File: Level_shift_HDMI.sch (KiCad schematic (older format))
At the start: 11 parts, among them U5 TXB0104RUT

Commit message: removed finished remarks
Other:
- note removed: "REMARK:Please unify convention of naming power supply labels.\nWe often use global labels. Always check that the name is exactly the same."
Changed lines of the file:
@@
 Wire Wire Line
 	7050 2150 7300 2150
-Text Notes 3650 975  0    50   ~ 0
-REMARK:Please unify convention of naming power supply labels.\nWe often use global labels. Always check that the name is exactly the same.
 $Comp
 L antmicroLogicTranslatorsLevelShifters:TXS0102YZPR U?

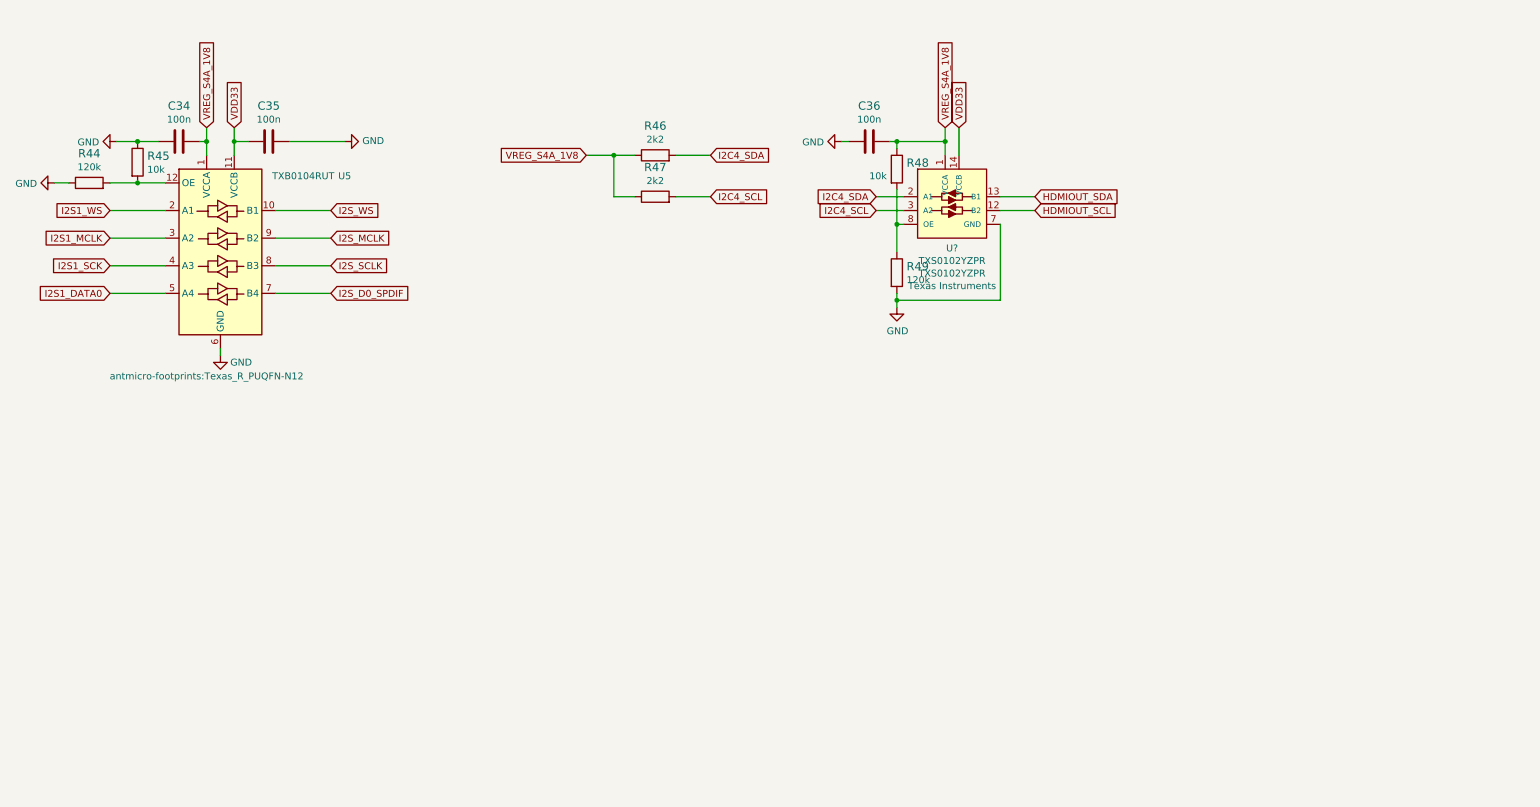
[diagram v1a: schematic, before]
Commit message: finished level shifting circuits for HDMI
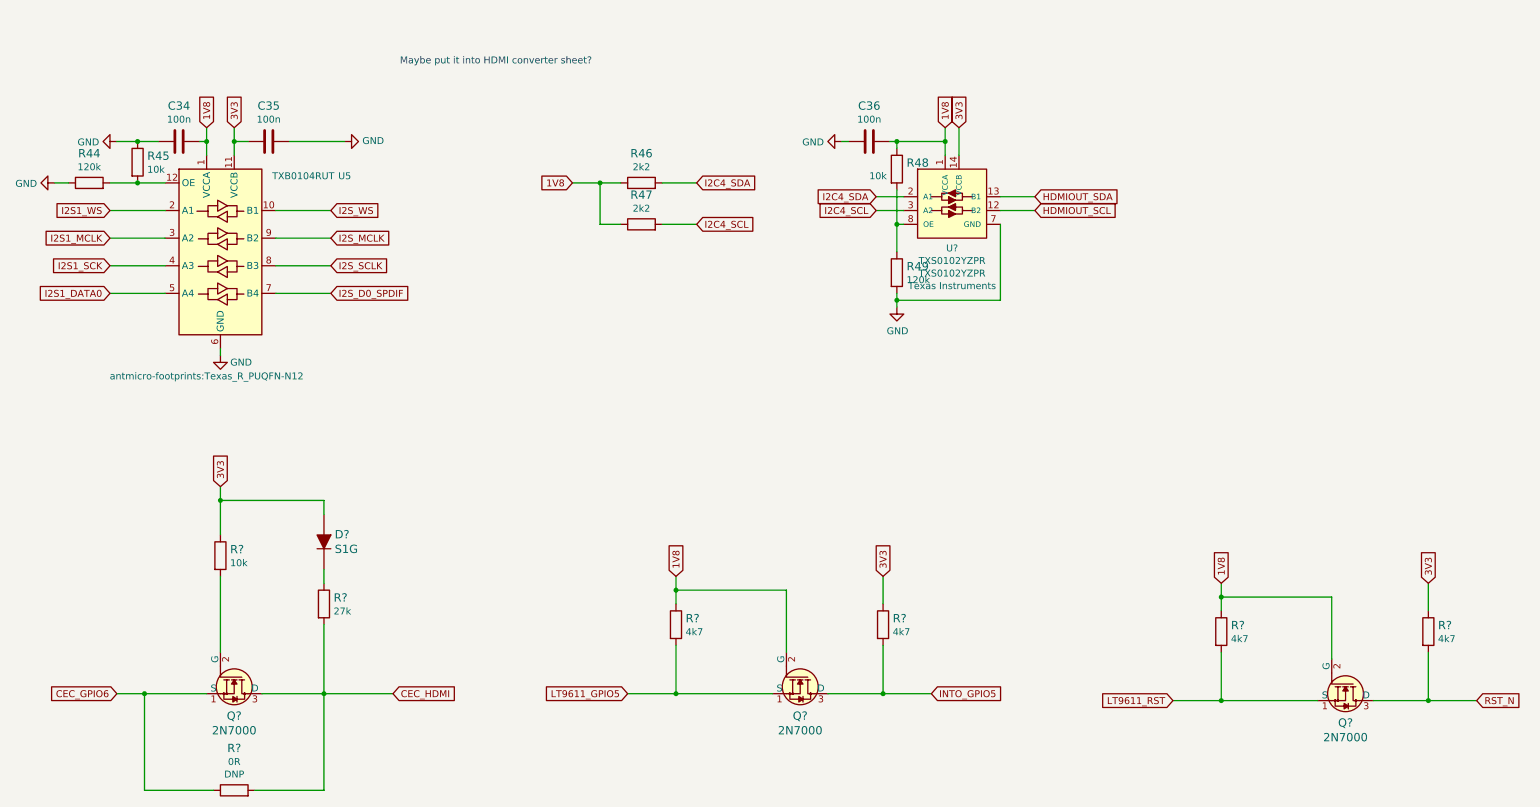
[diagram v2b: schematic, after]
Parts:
- added D?: S1G, antmicro-footprints:DO-214AC, symbol antmicroDiodesRectifiersSingle:S1G
- added Q? (x3): 2N7000, antmicro-footprints:TO-92-3, symbol antmicroTransistorsFETsMOSFETsSingle:2N7000
- added R? (x4): R_4k7_0402, antmicro-footprints:0402-res, symbol antmicroResistors0402:R_4k7_0402
- added R?: R_10k_0402, antmicro-footprints:0402-res, symbol antmicroResistors0402:R_10k_0402
- added R?: R_27k_0402, antmicro-footprints:0402-res, symbol antmicroResistors0402:R_27k_0402
- added R?: R_0R_0402, antmicro-footprints:0402-res, symbol antmicroResistors0402:R_0R_0402
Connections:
- net VDD33 renamed 3V3
- net 3V3: now also D?.A, R?.1, R?.1, R?.1
- net VREG_S4A_1V8 renamed 1V8
- net 1V8: now also Q?.2 (G), Q?.2 (G), R?.1, R?.1
- new net: Q?.2 (G), R?.2
- new net: D?.K, R?.1
- new net CEC_GPIO6: Q?.1 (S), R?.1
- new net CEC_HDMI: Q?.3 (D), R?.2, R?.2
- new net INTO_GPIO5: Q?.3 (D), R?.2
- new net LT9611_GPIO5: Q?.1 (S), R?.2
- new net LT9611_RST: Q?.1 (S), R?.2
- new net RST_N: Q?.3 (D), R?.2
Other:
- note added: "Maybe put it into HDMI converter sheet?\n"
- moved on the sheet: R46, R47

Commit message: Add local libs to fix CI
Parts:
- C34, C35, C36: footprint antmicro-footprints:0402-cap -> sa800u-baseboard-hw-footprints:0402-cap; symbol antmicroCapacitors0402:C_100n_0402 -> sa800u-baseboard-hw:C_100n_0402
- D?: footprint antmicro-footprints:DO-214AC -> sa800u-baseboard-hw-footprints:DO-214AC; symbol antmicroDiodesRectifiersSingle:S1G -> sa800u-baseboard-hw:S1G
- Q? (x3): footprint antmicro-footprints:TO-92-3 -> sa800u-baseboard-hw-footprints:TO-92-3; symbol antmicroTransistorsFETsMOSFETsSingle:2N7000 -> sa800u-baseboard-hw:2N7000
- R44, R49: footprint antmicro-footprints:0402-res -> sa800u-baseboard-hw-footprints:0402-res; symbol antmicroResistors0402:R_120k_0402 -> sa800u-baseboard-hw:R_120k_0402
- R45, R48: footprint antmicro-footprints:0603-res -> sa800u-baseboard-hw-footprints:0603-res; symbol antmicroResistors0603:R_10k_0603 -> sa800u-baseboard-hw:R_10k_0603
- R46, R47: footprint antmicro-footprints:0402-res -> sa800u-baseboard-hw-footprints:0402-res; symbol antmicroResistors0402:R_2k2_0402 -> sa800u-baseboard-hw:R_2k2_0402
- R? (x4): footprint antmicro-footprints:0402-res -> sa800u-baseboard-hw-footprints:0402-res; symbol antmicroResistors0402:R_4k7_0402 -> sa800u-baseboard-hw:R_4k7_0402
- R?: footprint antmicro-footprints:0402-res -> sa800u-baseboard-hw-footprints:0402-res; symbol antmicroResistors0402:R_10k_0402 -> sa800u-baseboard-hw:R_10k_0402
- R?: footprint antmicro-footprints:0402-res -> sa800u-baseboard-hw-footprints:0402-res; symbol antmicroResistors0402:R_27k_0402 -> sa800u-baseboard-hw:R_27k_0402
- R?: footprint antmicro-footprints:0402-res -> sa800u-baseboard-hw-footprints:0402-res; symbol antmicroResistors0402:R_0R_0402 -> sa800u-baseboard-hw:R_0R_0402
- U5: footprint antmicro-footprints:Texas_R_PUQFN-N12 -> sa800u-baseboard-hw-footprints:Texas_R_PUQFN-N12; symbol antmicroLogicTranslatorsLevelShifters:TXB0104RUT -> sa800u-baseboard-hw:TXB0104RUT
- U?: footprint antmicro-footprints:BGA8C50P2X4_88X188X50N -> sa800u-baseboard-hw-footprints:BGA8C50P2X4_88X188X50N; symbol antmicroLogicTranslatorsLevelShifters:TXS0102YZPR -> sa800u-baseboard-hw:TXS0102YZPR
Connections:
- net 1V8: now also U?.C1 (VCCA); no longer U?.1 (VCCA)
- net 3V3: now also U?.B2 (VCCB); no longer U?.14 (VCCB)
- net GND: now also U?.B1 (GND); no longer U?.7 (GND)
- net HDMIOUT_SCL: now also U?.A1 (B2); no longer U?.12 (B2)
- net HDMIOUT_SDA: now also U?.A2 (B1); no longer U?.13 (B1)
- net I2C4_SCL: now also U?.D1 (A2); no longer U?.3 (A2)
- net I2C4_SDA: now also U?.D2 (A1); no longer U?.2 (A1)
- net at R48.2, R49.1: now also U?.C2 (OE); no longer U?.8 (OE)
